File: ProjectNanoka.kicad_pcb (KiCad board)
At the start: 4 copper layers, 66 x 70 mm, 40 parts, among them J1 AUDIO_IN, J2 AUDIO OUT, J3 eBUTTON_4, J4 eBUTTON_3, J5 eBUTTON_2, J6 eBUTTON_1, J7 PWR_MOD_OUT, J8 12V_IN, J9 PWR_MOD_IN, K1 2-1462038-1, Q1 2SC1815, Q2 2SC1815, U1 TLV70033DDCR, U2 NC7WZ16P6X, U3 PS1440P02BT

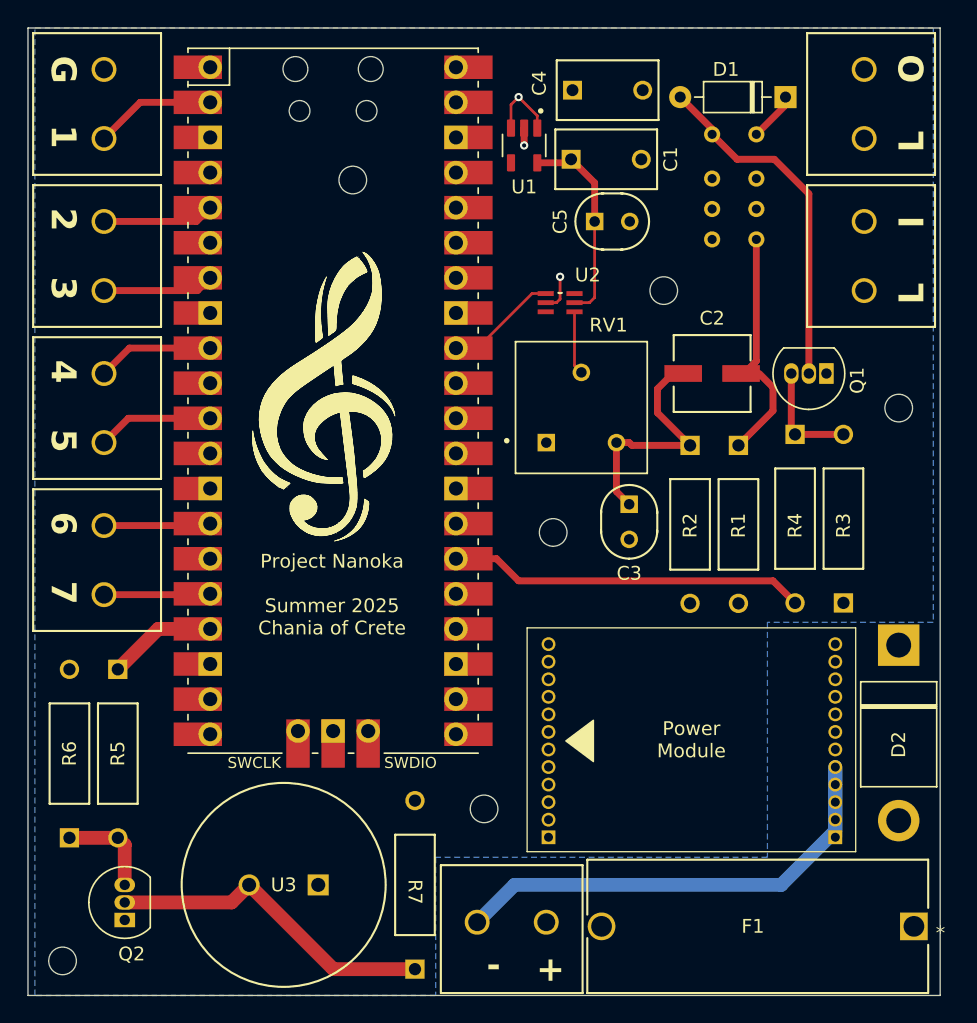
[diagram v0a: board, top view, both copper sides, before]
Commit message: Fix issues found in v1
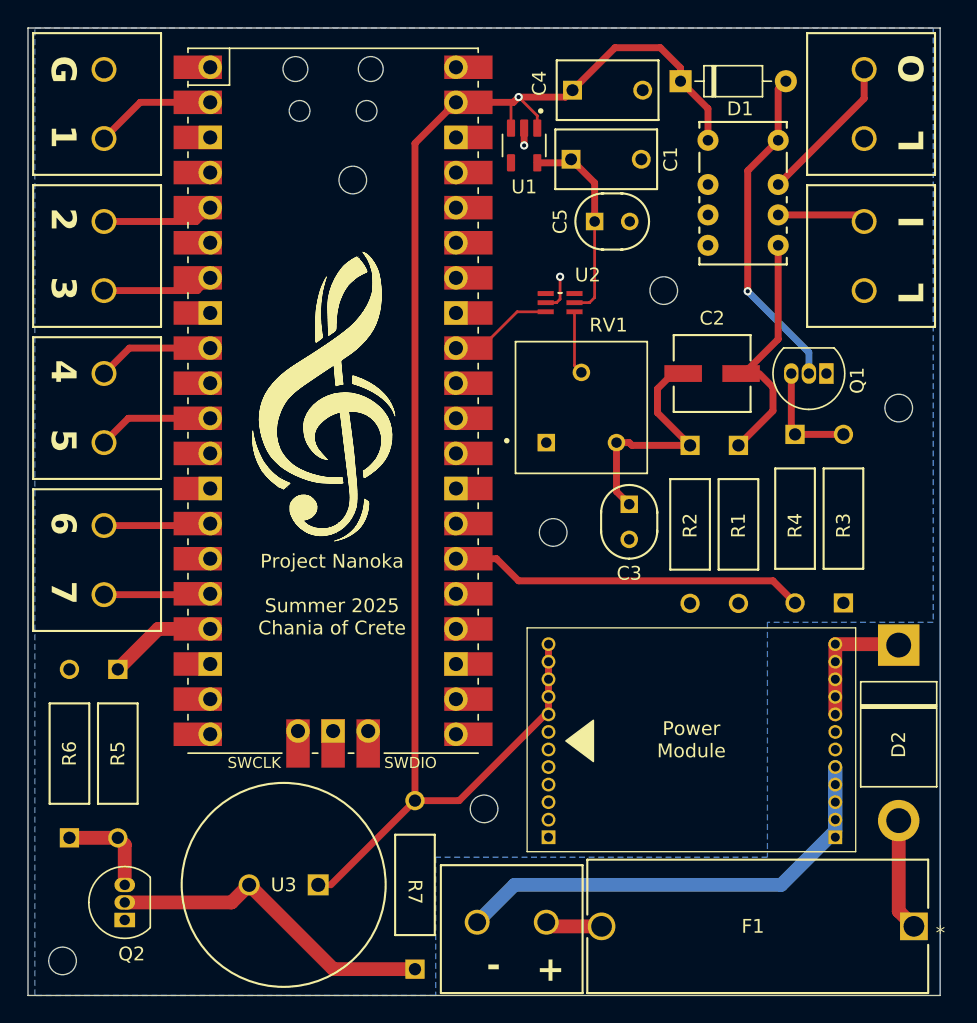
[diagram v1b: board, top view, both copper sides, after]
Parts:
- added G***: LOGO, Logos:cleff, B.Cu at (222.1, 67.7)
- A_IN1: renamed from J1; value AUDIO_IN -> ST_20A
- A_OUT1: renamed from J2; value AUDIO OUT -> ST_20A
- GT1: renamed from J6; value eBUTTON_1 -> ST_20A
- GT2: renamed from J5; value eBUTTON_2 -> ST_20A
- GT3: renamed from J4; value eBUTTON_3 -> ST_20A
- GT4: renamed from J3; value eBUTTON_4 -> ST_20A
- H1: renamed from J7; value PWR_MOD_OUT -> 1.27mm_12pin
- H2: renamed from J9; value PWR_MOD_IN -> 1.27mm_12pin
- K1: footprint Custom:RELAY8_THTNRW_TEC -> Custom:RELAY8-TH_NON-LATCH_1-COIL; moved to F.Cu
- P1: renamed from J8; value 12V_IN -> ST_20A
- RV1: value 1k -> 0-1k
- moved D1 7.68 mm to (246.7, 45.9), turned to 0 degrees
- moved K1 7.19 mm to (248.7, 50.1), turned to 0 degrees
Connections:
- A1 pad 34: S1 -> unconnected-(A1-GPIO28_ADC2-Pad34)
- A_IN1 pad 2: Net-(J1-Pin_2) -> AIN
- A_OUT1 pad 2: Net-(J2-Pin_2) -> AOUT
- C2 pad 2: Net-(C2-Pad2) -> PWM
- H1 pad 7: S1 -> unconnected-(H1-Pin_7-Pad7)
- K1 pad 2: Net-(J1-Pin_2) -> unconnected-(K1-Pad2)
- K1 pad 3: Net-(J2-Pin_2) -> unconnected-(K1-Pad3)
- K1 pad 4: Net-(C2-Pad2) -> unconnected-(K1-Pad4)
- K1 pad 5: unconnected-(K1-Pad5) -> PWM
- K1 pad 6: unconnected-(K1-Pad6) -> AOUT
- K1 pad 7: unconnected-(K1-Pad7) -> AIN
- R1 pad 1: Net-(C2-Pad2) -> PWM
- U2 pad 1: Net-(A1-GPIO27_ADC1) -> unconnected-(U2-A1-Pad1)
- U2 pad 3: unconnected-(U2-A2-Pad3) -> Net-(A1-GPIO27_ADC1)
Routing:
- net S1: track 37.1 -> 0.00 mm
- net PWM: track 0.00 -> 17.2 mm
- net Net-(C2-Pad2): track 16.9 -> 0.00 mm
- net Net-(J1-Pin_2): track 11.1 -> 0.00 mm
- net AIN: track 0.00 -> 10.9 mm
- net Net-(J2-Pin_2): track 8.17 -> 0.00 mm
- net +5V: track 114.1 -> 107.5 mm
- net AOUT: track 0.00 -> 6.42 mm
- net Net-(D1-A): track 25.4 -> 24.1 mm, vias 0 -> 1
- net Net-(D2-K): track 10.4 -> 9.70 mm
- net Net-(A1-GPIO27_ADC1): track 8.13 -> 7.58 mm
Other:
- copper layers 4 -> 2

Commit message: Make improvements to board
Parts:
- A1: footprint Custom:RPi_Pico_SMD_TH -> Footprints:RPi_Pico_SMD_TH
- A_IN1, A_OUT1, GT1, GT2, GT3, GT4, P1: footprint Custom:CONN_1935161_PXC -> Footprints:CONN_1935161_PXC
- C1, C4: footprint Custom:CAP_C330C_MR_X7R_KEM -> Footprints:CAP_C330C_MR_X7R_KEM
- C2: footprint Custom:CAP_UUQ_5X5P4_NCH -> Footprints:CAP_UUQ_5X5P4_NCH
- C3, C5: footprint Custom:CAP_C320_KEM -> Footprints:CAP_C320_KEM
- D1: footprint Diode_THT:D_DO-35_SOD27_P7.62mm_Horizontal -> Footprints:D_DO-35_SOD27_P7.62mm_Horizontal
- D2: footprint Custom:P33_D5.4x7.5 -> Footprints:P33_D5.4x7.5
- F1: footprint Custom:20x300_FUSE_HOLDER_0PTF0078P_LTF -> Footprints:20x300_FUSE_HOLDER_0PTF0078P_LTF
- G*** (x3): footprint Logos:cleff -> Footprints:cleff
- H1, H2: footprint Custom:PinHeader_1x12_P1.27mm_Vertical_Modded -> Footprints:PinHeader_1x12_P1.27mm_Vertical_Modded
- K1: footprint Custom:RELAY8-TH_NON-LATCH_1-COIL -> Footprints:RELAY8-TH_NON-LATCH_1-COIL
- Q1, Q2: footprint Package_TO_SOT_THT:TO-92_Inline -> Footprints:TO-92_Inline
- R1, R2: footprint Custom:STA_CF14_STP -> Footprints:STA_CF14_STP
- R3, R4, R5, R6, R7: footprint Custom:STA_RNF14_STP -> Footprints:STA_RNF14_STP
- REF** (x6): footprint MountingHole:MountingHole_2mm -> Footprints:MountingHole_2mm
- RV1: footprint Custom:TRIM_3310Y-101-102L -> Footprints:TRIM_3310Y-101-102L
- U1: footprint Custom:SOT95P280X110-5N -> Footprints:SOT95P280X110-5N
- U2: footprint Custom:SOT65P210X110-6N -> Footprints:SOT65P210X110-6N
- U3: footprint Custom:PS1440P02BT_TDK -> Footprints:PS1440P02BT_TDK
- moved U3 3.91 mm to (217.5, 101.5), turned to -90 degrees
- moved GT4 1.50 mm to (205.0, 76.5)
- moved GT3 1.00 mm to (205.0, 66.0)
- moved A_OUT1 0.50 mm to (260.0, 60.5)
- moved GT2 0.50 mm to (205.0, 55.5)
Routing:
- net +5V: track 107.5 -> 111.3 mm
- net Net-(Q2-C): track 24.1 -> 23.0 mm
- net Net-(A1-GPIO10): track 7.74 -> 8.45 mm
- net Net-(A1-GPIO12): track 7.71 -> 8.37 mm
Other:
- board text added: "220ohm min"
- board text added: "IN"
- board text added: "OUT"
- board text added: "Pull down resistors required"
- board text added: "Rev 1.1"
- board text removed: "I"
- board text removed: "L"
- board text removed: "O"

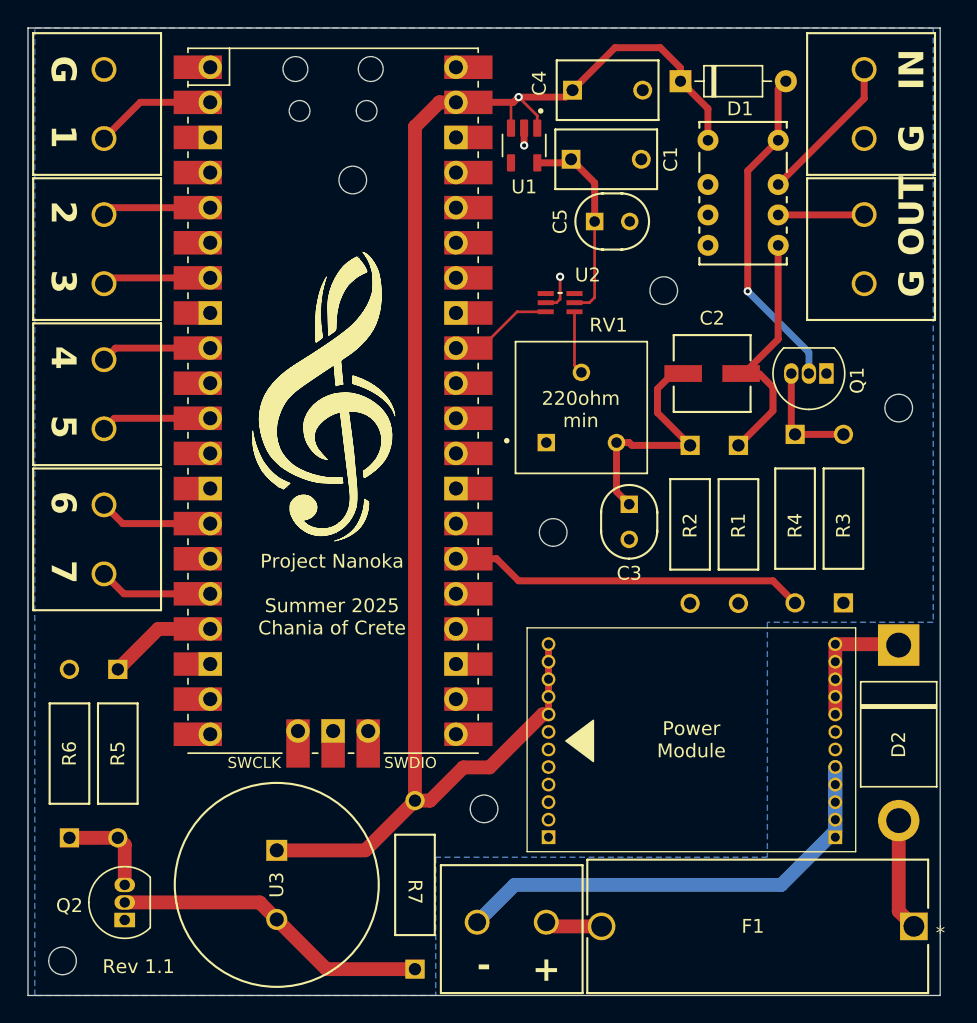
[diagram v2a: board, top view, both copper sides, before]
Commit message: Replaced 2SC1815 with 2N3904BU
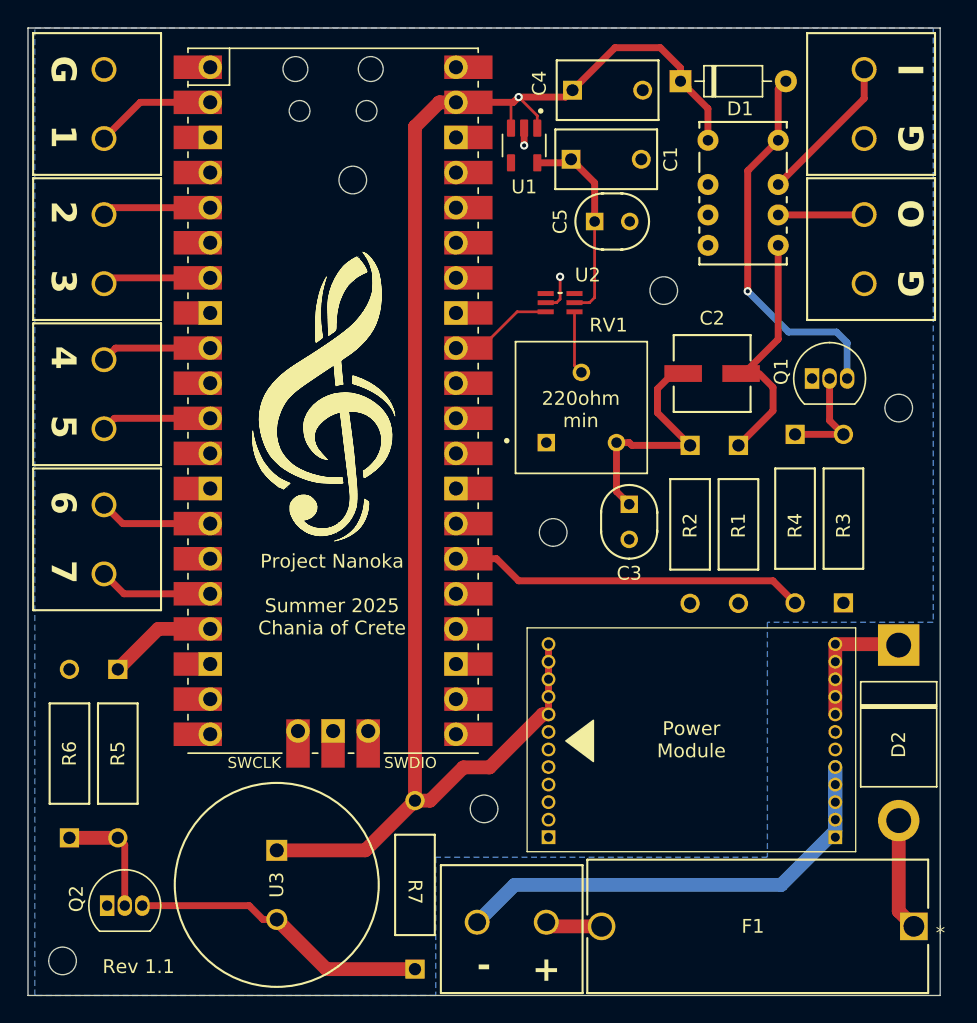
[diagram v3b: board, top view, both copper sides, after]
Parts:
- Q1, Q2: value 2SC1815 -> 2N3904BU; footprint Footprints:TO-92_Inline -> Footprints:2N3904BU
- R4, R5: value 270 -> 1k
- moved Q2 1.64 mm to (205.2, 105.5), turned to 0 degrees
- moved Q1 1.10 mm to (256.2, 67.4), turned to 0 degrees
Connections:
- R3 pad 2: Net-(Q1-B) -> Net-(Q1-PadB)
- R4 pad 1: Net-(Q1-B) -> Net-(Q1-PadB)
- R5 pad 2: Net-(Q2-B) -> Net-(Q2-PadB)
- R6 pad 1: Net-(Q2-B) -> Net-(Q2-PadB)
- R7 pad 1: Net-(Q2-C) -> Net-(Q2-PadC)
- U3 pad 2: Net-(Q2-C) -> Net-(Q2-PadC)
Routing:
- net Net-(Q2-C): track 23.0 -> 0.00 mm
- net Net-(Q2-PadC): track 0.00 -> 21.6 mm
- net Net-(Q2-PadB): track 0.00 -> 8.61 mm
- net Net-(Q1-PadB): track 0.00 -> 8.34 mm
- net Net-(Q1-B): track 8.02 -> 0.00 mm
- net Net-(Q2-B): track 7.11 -> 0.00 mm
- net Net-(D1-A): track 24.1 -> 27.7 mm
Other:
- board text added: "I"
- board text added: "O"
- board text removed: "IN"
- board text removed: "OUT"

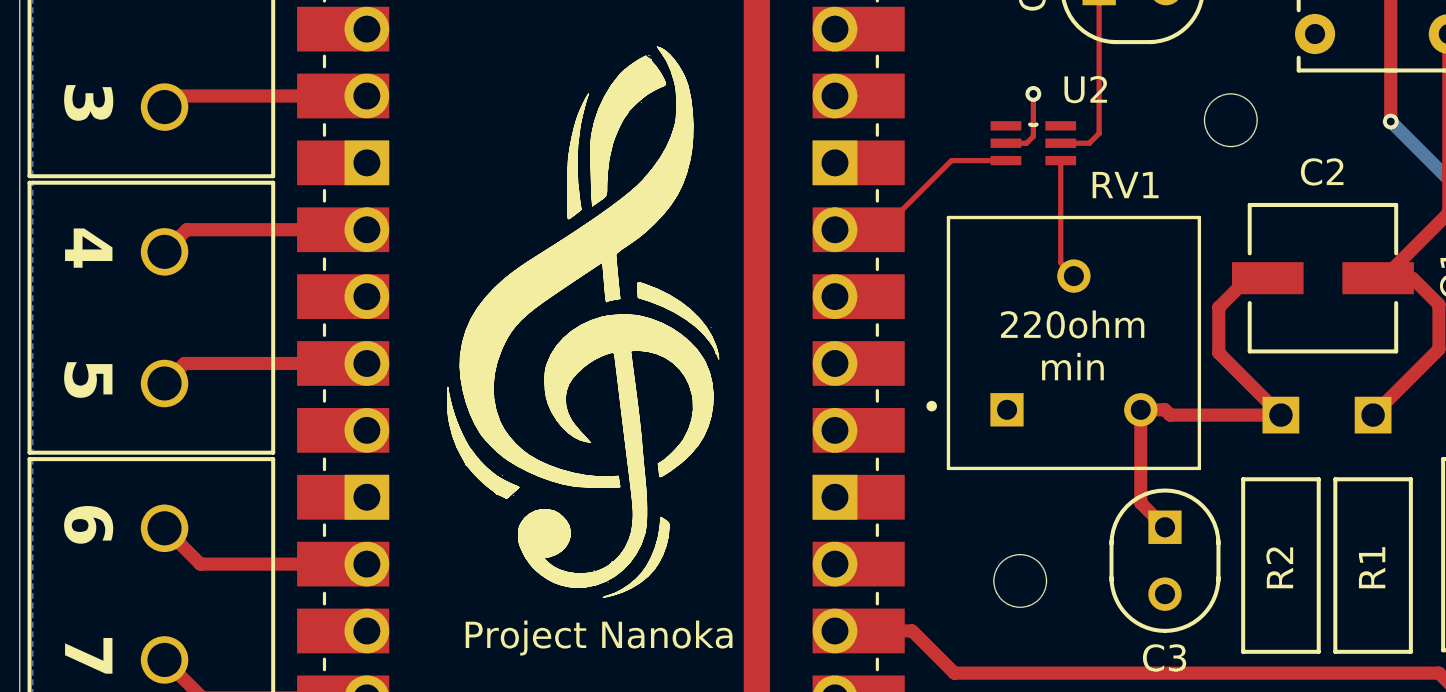
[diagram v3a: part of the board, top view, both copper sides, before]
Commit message: Replaced RV1 with a 220ohm resistor
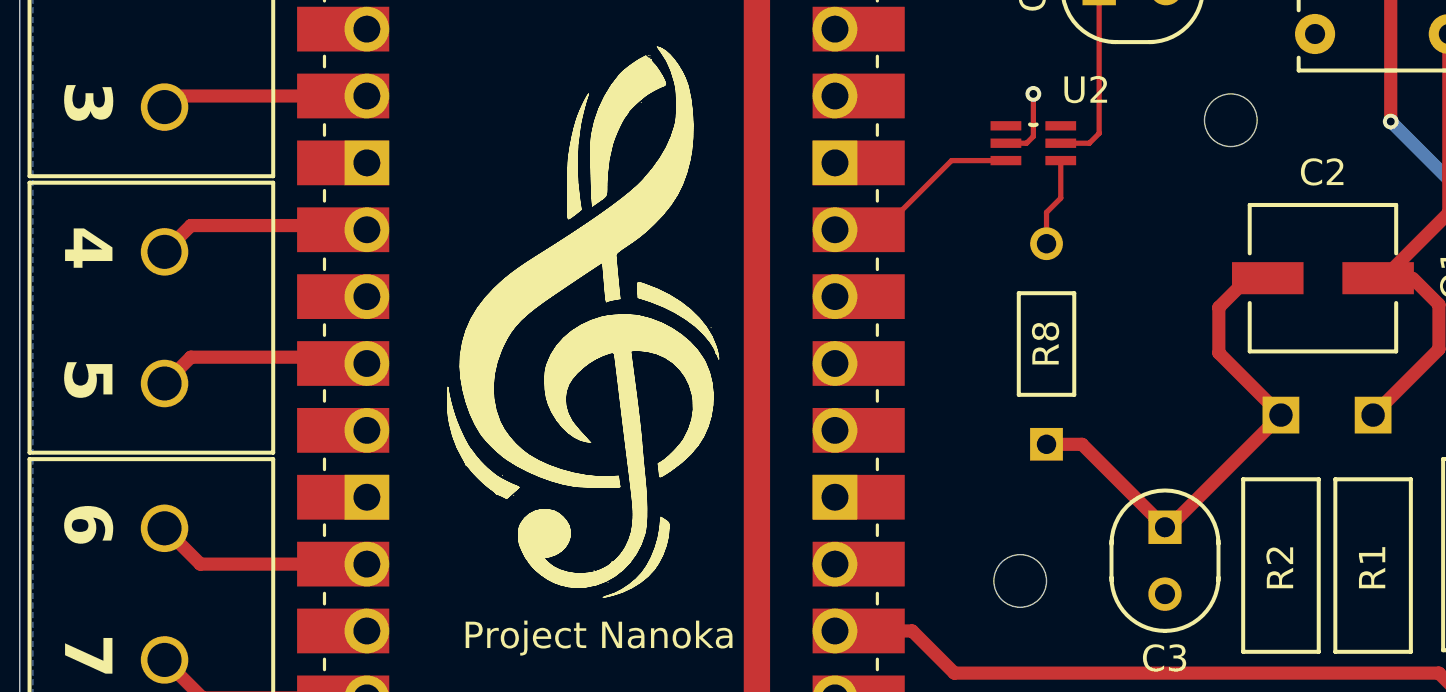
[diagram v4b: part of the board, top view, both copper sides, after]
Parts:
- removed RV1: 0-1k, Footprints:TRIM_3310Y-101-102L
- added R8: 220, Footprints:STA_RNMF14_STP, F.Cu at (238.5, 73.3)
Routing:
- net Net-(C2-Pad1): track 16.9 -> 18.6 mm
- net Net-(U2-Y2): track 4.59 -> 3.38 mm
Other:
- board text removed: "220ohm min"
